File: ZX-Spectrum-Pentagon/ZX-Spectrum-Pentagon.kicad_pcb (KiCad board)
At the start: 2 copper layers, 213.1 x 129 mm, 250 parts, among them U1 74HC04, U10 74HC193, U11 74HC02, U12 74HC08, U13 74HC74, U14 74HC393, U15 74HC74, U16 74HC273, U17 74HC257, U18 74HC273, U19 AY-3-8910, U2 74HC14, U20 AY-3-8912_DUMMY, U21 AY-3-8913_DUMMY, U22 LM311, U23 74HC244, U25 74HC541, U26 74HC541, U27 Z80CPU, U28 74HC244, U29 GAL16V8, U3 74HC93, U30 29F040, U31 74HC32, U32 74HC00, U33 74HC74, U34 74HC08, U35 74HC574, U36 74HC574, U37 74HC153, U38 74HC153, U39 GAL16V8, U4 74HC11, U40 74HC574, U41 74HC166, U42 74HC257, U43 74HC541, U44 HM628512, U45 74HC574, U46 74HC257, U47 74HC257, U48 74HC257, U49 74HC08, U5 74HC193, U50 AD724, U6 74HC257, U7 74HC04, U8 74HC00, U9 74HC86

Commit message: non functional changes
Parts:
- SWIO1: value SW_Push_DPDT -> ABC/ACB
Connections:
- SWIO1 pad 7: (no net) -> GND
- SWIO1 pad 8: (no net) -> GND
- SWIO2 pad 7: (no net) -> GND
- SWIO2 pad 8: (no net) -> GND
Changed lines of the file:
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@@
     (pad "6" thru_hole circle (at 1.5 3.2) (size 1.4 1.4) (drill 0.762) (layers *.Cu *.Mask)
       (net 185 "unconnected-(SWIO2-Pad6)") (pinfunction "C") (pintype "passive+no_connect"))
-    (pad "7" thru_hole circle (at -3.4 -5.9) (size 1.4 1.4) (drill 0.762) (layers *.Cu *.Mask))
-    (pad "8" thru_hole circle (at 3.4 5.9) (size 1.4 1.4) (drill 0.762) (layers *.Cu *.Mask))
+    (pad "7" thru_hole circle (at -3.4 -5.9) (size 1.4 1.4) (drill 0.762) (layers *.Cu *.Mask)
+      (net 4 "GND") (pintype "passive"))
+    (pad "8" thru_hole circle (at 3.4 5.9) (size 1.4 1.4) (drill 0.762) (layers *.Cu *.Mask)
+      (net 4 "GND") (pintype "passive"))
   )
   (footprint "Capacitor_Tantalum_SMD:CP_EIA-7343-31_Kemet-D_Pad2.25x2.55mm_HandSolder" (layer "F.Cu")
@@
       (effects (font (size 1 1) (thickness 0.15)))
     )
-    (fp_text value "SW_Push_DPDT" (at 0 9.2 unlocked) (layer "F.Fab") hide
+    (fp_text value "ABC/ACB" (at 0 9.2 unlocked) (layer "F.Fab") hide
       (effects (font (size 1 1) (thickness 0.15)))
     )
@@
     (pad "6" thru_hole circle (at 1.5 3.2) (size 1.4 1.4) (drill 0.762) (layers *.Cu *.Mask)
       (net 182 "/InputOutput/CHB") (pinfunction "C") (pintype "passive"))
-    (pad "7" thru_hole circle (at -3.4 -5.9) (size 1.4 1.4) (drill 0.762) (layers *.Cu *.Mask))
-    (pad "8" thru_hole circle (at 3.4 5.9) (size 1.4 1.4) (drill 0.762) (layers *.Cu *.Mask))
+    (pad "7" thru_hole circle (at -3.4 -5.9) (size 1.4 1.4) (drill 0.762) (layers *.Cu *.Mask)
+      (net 4 "GND") (pintype "passive"))
+    (pad "8" thru_hole circle (at 3.4 5.9) (size 1.4 1.4) (drill 0.762) (layers *.Cu *.Mask)
+      (net 4 "GND") (pintype "passive"))
   )
   (footprint "Package_DIP:DIP-16_W7.62mm" (layer "F.Cu")

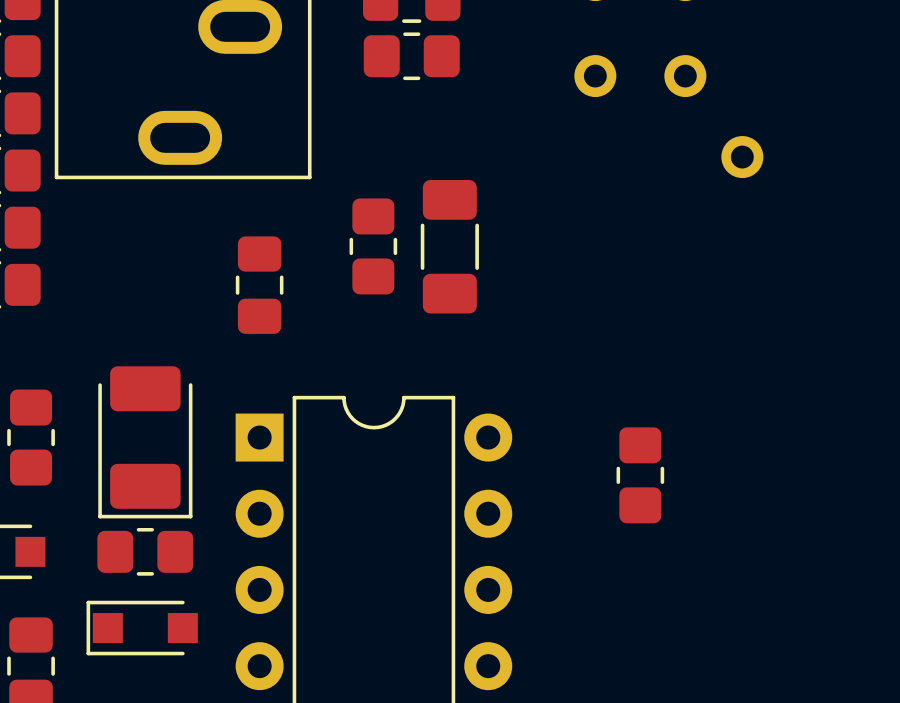
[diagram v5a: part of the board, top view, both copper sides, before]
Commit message: reposition companents
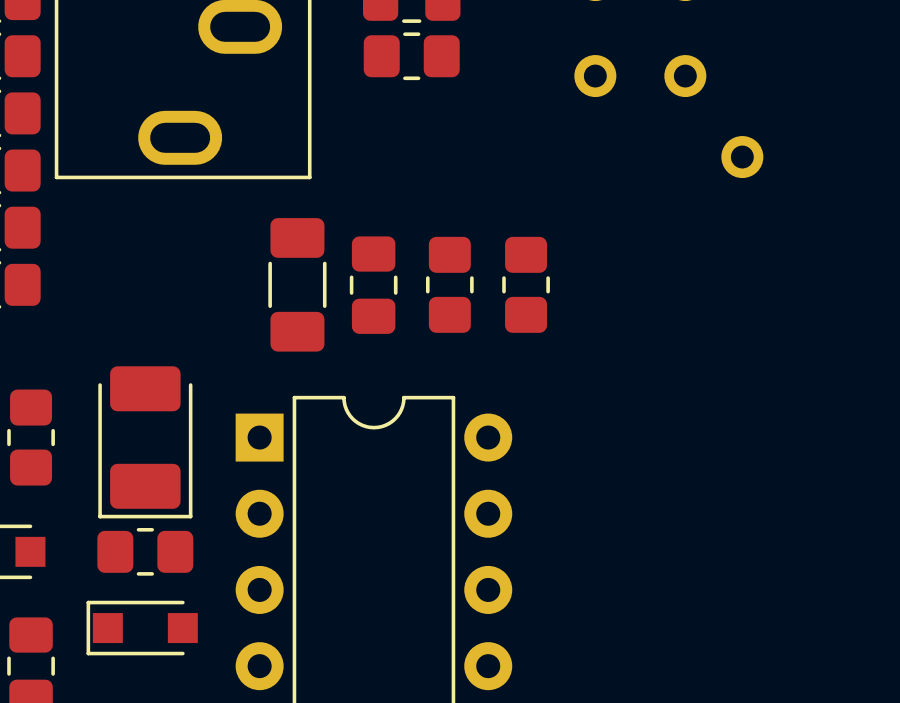
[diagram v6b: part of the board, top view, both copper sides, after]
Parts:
- moved RIO5 8.98 mm to (86.4, 38.1)
- moved RIO6 5.25 mm to (88.9, 38.1), turned to -90 degrees
- moved CPF22 5.24 mm to (81.3, 38.1)
- moved CIO11 3.80 mm to (83.8, 38.1)
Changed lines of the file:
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@@
   )
   (footprint "Resistor_SMD:R_0805_2012Metric_Pad1.20x1.40mm_HandSolder" (layer "F.Cu")
-    (at 92.71 44.45 90)
+    (at 86.36 38.1 90)
     (descr "Resistor SMD 0805 (2012 Metric), square (rectangular) end terminal, IPC_7351 nominal with elongated pad for handsoldering. (Body size source: IPC-SM-782 page 72, https://www.pcb-3d.com/wordpress/wp-content/uploads/ipc-sm-782a_amendment_1_and_2.pdf), generated with kicad-footprint-generator")
     (tags "resistor handsolder")
@@
   )
   (footprint "Resistor_SMD:R_0805_2012Metric_Pad1.20x1.40mm_HandSolder" (layer "F.Cu")
-    (at 83.81 36.82 90)
+    (at 88.9 38.1 -90)
     (descr "Resistor SMD 0805 (2012 Metric), square (rectangular) end terminal, IPC_7351 nominal with elongated pad for handsoldering. (Body size source: IPC-SM-782 page 72, https://www.pcb-3d.com/wordpress/wp-content/uploads/ipc-sm-782a_amendment_1_and_2.pdf), generated with kicad-footprint-generator")
     (tags "resistor handsolder")
@@
     (fp_line (start -1 -0.625) (end 1 -0.625) (layer "F.Fab") (width 0.1))
     (fp_line (start 1 -0.625) (end 1 0.625) (layer "F.Fab") (width 0.1))
-    (pad "1" smd roundrect (at -1 0 90) (size 1.2 1.4) (layers "F.Cu" "F.Paste" "F.Mask") (roundrect_rratio 0.208333)
+    (pad "1" smd roundrect (at -1 0 270) (size 1.2 1.4) (layers "F.Cu" "F.Paste" "F.Mask") (roundrect_rratio 0.208333)
       (net 9 "VCC") (pintype "passive"))
-    (pad "2" smd roundrect (at 1 0 90) (size 1.2 1.4) (layers "F.Cu" "F.Paste" "F.Mask") (roundrect_rratio 0.208333)
+    (pad "2" smd roundrect (at 1 0 270) (size 1.2 1.4) (layers "F.Cu" "F.Paste" "F.Mask") (roundrect_rratio 0.208333)
       (net 19 "Net-(CIO10-Pad1)") (pintype "passive"))
     (model "${KICAD6_3DMODEL_DIR}/Resistor_SMD.3dshapes/R_0805_2012Metric.wrl"
@@
   )
   (footprint "Capacitor_SMD:C_0805_2012Metric_Pad1.18x1.45mm_HandSolder" (layer "F.Cu")
-    (at 80.02 38.11 -90)
+    (at 83.82 38.11 -90)
     (descr "Capacitor SMD 0805 (2012 Metric), square (rectangular) end terminal, IPC_7351 nominal with elongated pad for handsoldering. (Body size source: IPC-SM-782 page 76, https://www.pcb-3d.com/wordpress/wp-content/uploads/ipc-sm-782a_amendment_1_and_2.pdf, https://docs.google.com/spreadsheets/d/1BsfQQcO9C6DZCsRaXUlFlo91Tg2WpOkGARC1WS5S8t0/edit?usp=sharing), generated with kicad-footprint-generator")
     (tags "capacitor handsolder")
@@
   )
   (footprint "Capacitor_SMD:C_1206_3216Metric_Pad1.33x1.80mm_HandSolder" (layer "F.Cu")
-    (at 86.36 36.83 90)
+    (at 81.28 38.1 90)
     (descr "Capacitor SMD 1206 (3216 Metric), square (rectangular) end terminal, IPC_7351 nominal with elongated pad for handsoldering. (Body size source: IPC-SM-782 page 76, https://www.pcb-3d.com/wordpress/wp-content/uploads/ipc-sm-782a_amendment_1_and_2.pdf), generated with kicad-footprint-generator")
     (tags "capacitor handsolder")

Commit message: reposition companent
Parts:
- removed SWIO2: SW_Push_DPDT, ZX-Spectrum-Pentagon:PS-22F03
- added SWVF1: 128K/512K, ZX-Spectrum-Pentagon:PS-22F03, F.Cu at (116.8, 27.9)
- moved U23 382.3 mm to (44.5, 90.2), turned to 90 degrees
- moved RSIO1 349.4 mm to (45.7, 94.0)
- moved JIOB1 339.6 mm to (118.1, 76.2), turned to 90 degrees
- moved CPF20 338.0 mm to (85.1, 74.9), turned to 90 degrees
- moved CPF19 332.7 mm to (82.5, 74.9), turned to 90 degrees
- moved JIO1 325.4 mm to (400.1, 78.7)
- moved U20 322.4 mm to (91.5, 67.3), turned to 90 degrees
- moved U19 320.3 mm to (83.8, 69.8), turned to 90 degrees
- moved U21 311.0 mm to (116.8, 57.1), turned to -90 degrees
- moved CPF21 307.8 mm to (121.9, 49.5)
- moved JIOA1 299.9 mm to (96.5, 76.2), turned to 90 degrees
- moved LIO1 294.8 mm to (138.4, 66.0), turned to 90 degrees
- moved CIO1 294.0 mm to (137.2, 57.1), turned to 90 degrees
- moved CIO2 287.7 mm to (141.0, 57.1), turned to 90 degrees
- moved JIO4 54.8 mm to (68.6, 97.8), turned to -90 degrees

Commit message: reposition companents
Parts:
- locked: footprint Package_DIP:DIP-22_W7.62mm -> Package_DIP:DIP-20_W7.62mm
- moved U1 299.8 mm to (43.2, 146.0), turned to 90 degrees
- moved U14 295.5 mm to (111.8, 146.0), turned to 90 degrees
- moved U13 292.4 mm to (134.6, 146.0), turned to 90 degrees
- moved U5 285.7 mm to (28.0, 133.3), turned to 90 degrees
- moved U11 280.9 mm to (104.1, 133.3), turned to 90 degrees
- moved U6 280.1 mm to (78.8, 133.3), turned to 90 degrees
- moved CPF1 276.7 mm to (39.4, 139.7), turned to -90 degrees
- moved CPF19 274.5 mm to (12.7, -190.5), turned to 0 degrees
- moved U3 273.4 mm to (66.7, 146.0), turned to 90 degrees
- moved CPF20 272.7 mm to (12.7, -188.0), turned to 0 degrees
- moved CPF14 271.5 mm to (107.9, 139.7), turned to -90 degrees
- moved U19 267.4 mm to (17.8, -189.2), turned to 0 degrees
- moved CPF13 267.1 mm to (130.8, 140.0), turned to -90 degrees
- moved JIOA1 266.7 mm to (11.4, -176.5), turned to 0 degrees
- moved U7 266.0 mm to (160.0, 146.0), turned to 90 degrees
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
